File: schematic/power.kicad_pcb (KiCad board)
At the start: 2 copper layers, 76.7 x 52.7 mm, 21 parts, among them J1 Conn_01x02, J2 Conn_01x02, J3 Conn_01x02, J4 Conn_01x02, J5 Conn_02x06_Odd_Even, U1 LM2595S-3.3, U2 INA219AxD

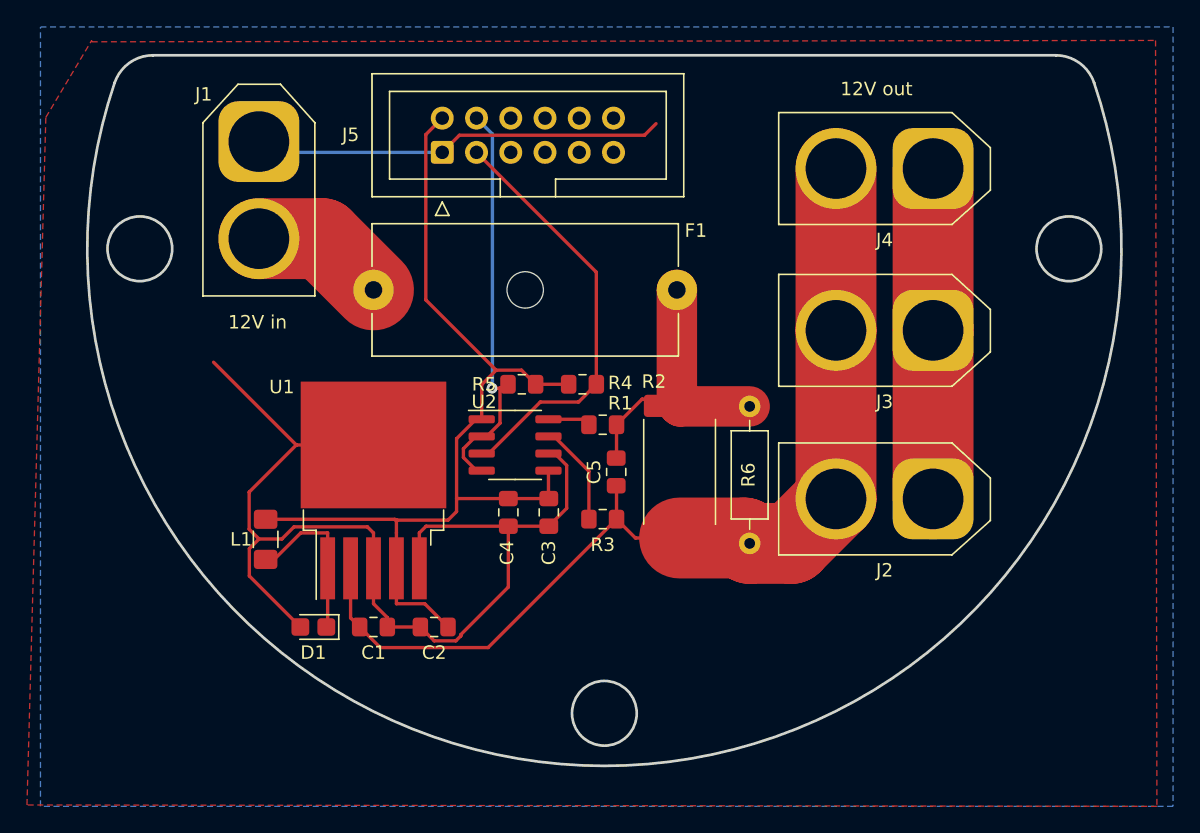
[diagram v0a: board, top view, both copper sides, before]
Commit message: correct power D1, C1, C2 and L1 footprint. accurate L1, D1 and C2 values
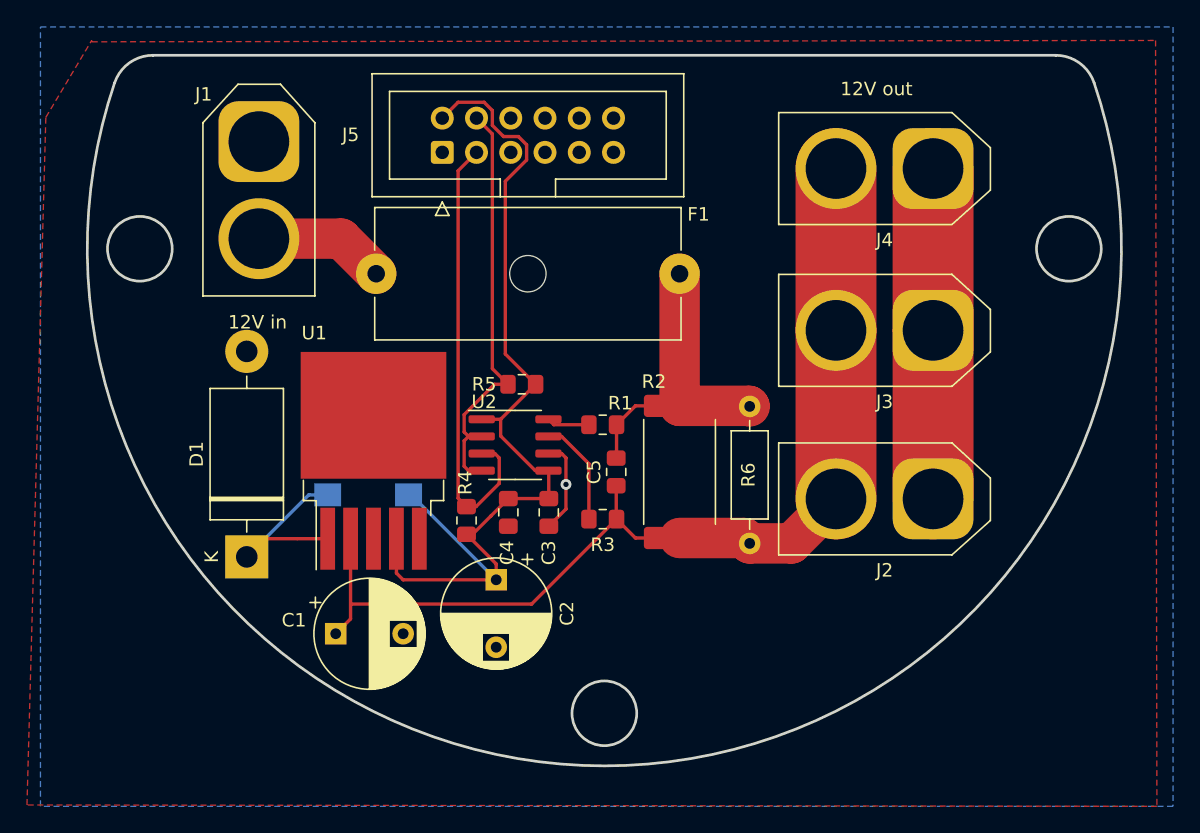
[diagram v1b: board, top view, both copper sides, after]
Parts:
- C1: value C680uF -> CP; footprint Capacitor_SMD:C_0805_2012Metric_Pad1.15x1.40mm_HandSolder -> Capacitor_THT:CP_Radial_D8.0mm_P5.00mm
- C2: footprint Capacitor_SMD:C_0805_2012Metric_Pad1.15x1.40mm_HandSolder -> Capacitor_THT:CP_Radial_D8.0mm_P5.00mm
- D1: value D -> 1N5822; footprint Diode_SMD:D_0805_2012Metric_Castellated -> Diode_THT:D_DO-201AD_P15.24mm_Horizontal
- L1: value L33uH -> 68uH; footprint Inductor_SMD:L_1206_3216Metric_Pad1.42x1.75mm_HandSolder -> Inductor_SMD:L_Wuerth_WE-PD-Typ-7345; moved to B.Cu
- moved R4 13.3 mm to (142.9, 114.6), turned to 270 degrees
- moved L1 8.29 mm to (135.6, 112.7), turned to 0 degrees
- moved D1 7.17 mm to (126.6, 117.3), turned to 90 degrees
- moved C2 5.78 mm to (145.1, 119.0), turned to 270 degrees
- moved C1 2.84 mm to (133.2, 123.0)
- moved U1 2.20 mm to (136.0, 110.2)
- moved F1 1.22 mm to (158.7, 96.3)
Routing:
- net GND: track 138.0 -> 31.5 mm, vias 0 -> 1
- net I2C-SDA: track 31.5 -> 33.6 mm
- net Net-(D1-Pad1): track 12.4 -> 14.5 mm
- net +12V: track 73.6 -> 75.2 mm
- net +3V3: track 73.2 -> 71.8 mm
- net Net-(C5-Pad2): track 21.6 -> 22.8 mm
- net I2C-SCL: track 30.3 -> 31.4 mm, vias 1 -> 0
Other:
- board text added: "Aruna power github.com/aruna-rov"
- board text removed: "Aruna power github.com/aruna"

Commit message: added version
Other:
- board text added: "Aruna - Power github.com/aruna-rov/Apsu V1"
- board text removed: "Aruna power github.com/aruna-rov"

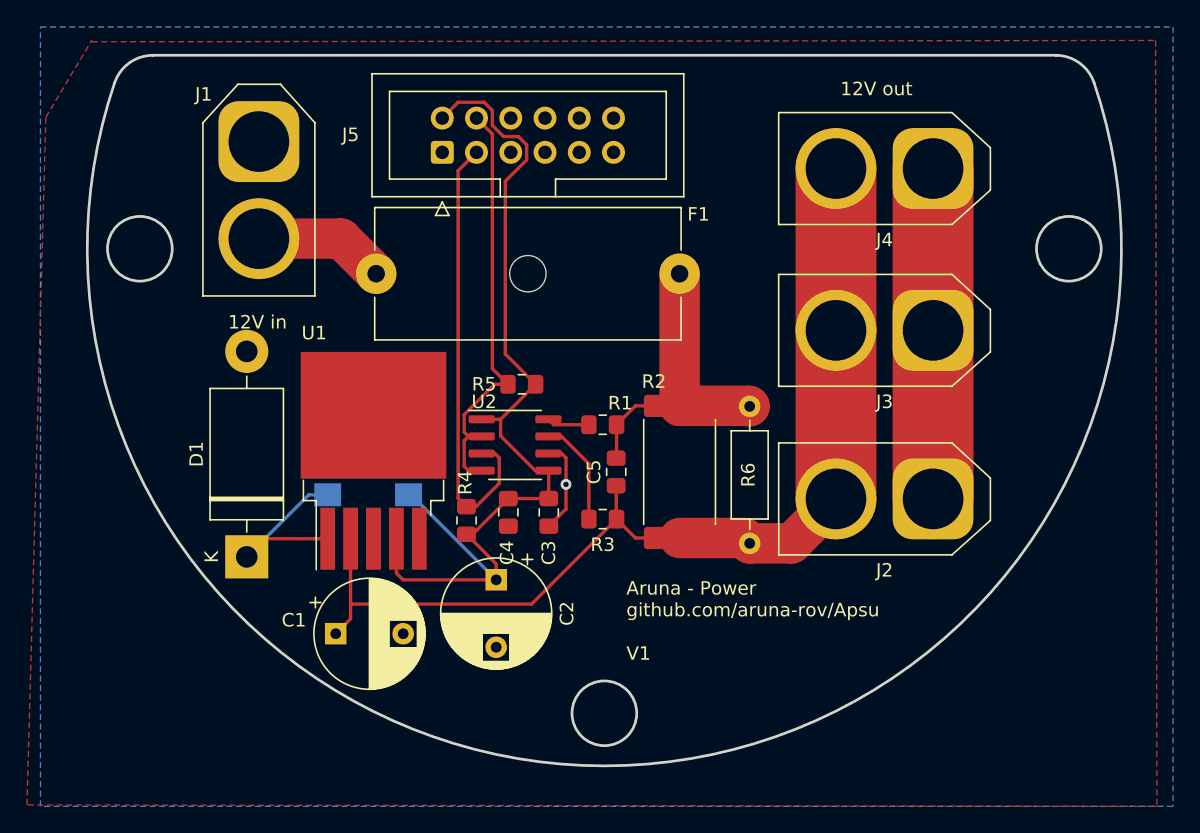
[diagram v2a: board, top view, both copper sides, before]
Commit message: added MPN for connectors
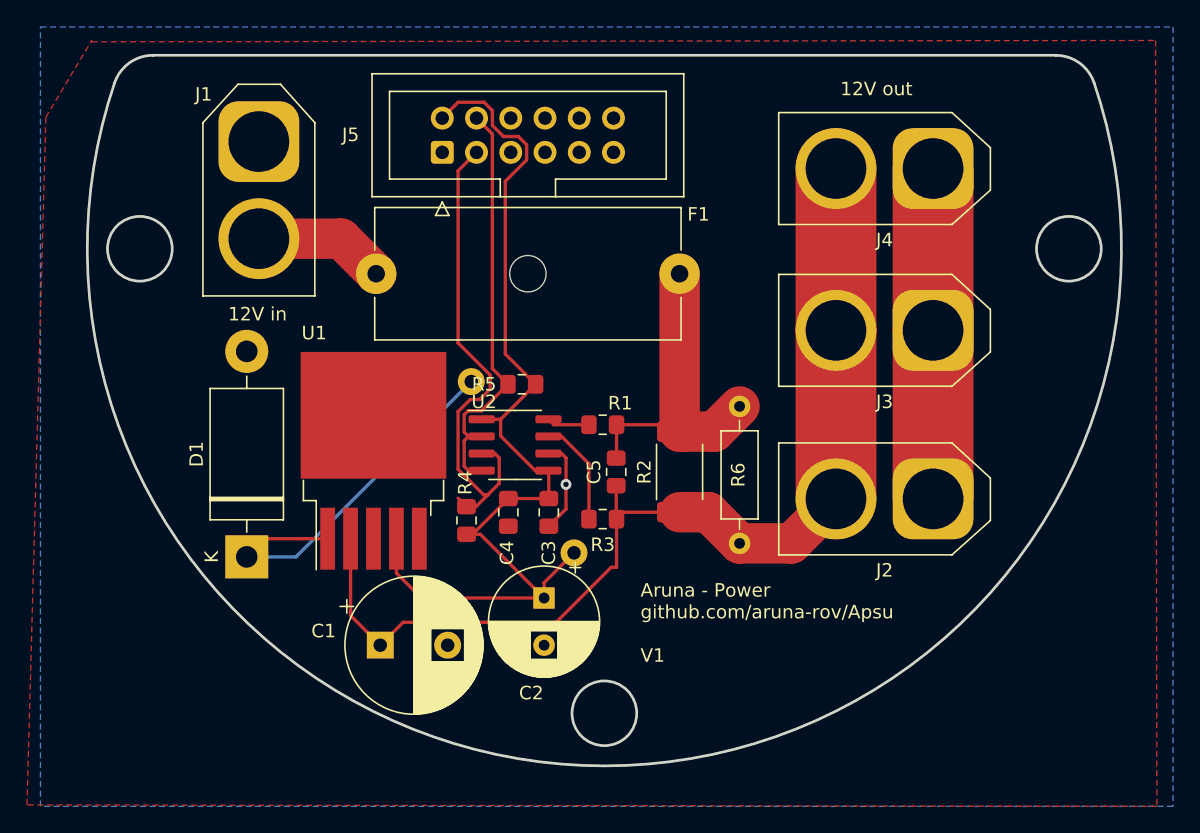
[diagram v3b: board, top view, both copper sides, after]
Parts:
- C1: value CP -> 100uF; footprint Capacitor_THT:CP_Radial_D8.0mm_P5.00mm -> Capacitor_THT:CP_Radial_D10.0mm_P5.00mm
- C2: value C220uF -> 220uF; footprint Capacitor_THT:CP_Radial_D8.0mm_P5.00mm -> Capacitor_THT:CP_Radial_D8.0mm_P3.50mm
- L1: footprint Inductor_SMD:L_Wuerth_WE-PD-Typ-7345 -> Inductor_THT:L_Radial_L16.1mm_W16.1mm_Px7.62mm_Py12.70mm_Pulse_LP-44
- R2: footprint Resistor_SMD:R_4020_10251Metric_Pad1.65x5.30mm_HandSolder -> Resistor_SMD:R_2512_6332Metric_Pad1.52x3.35mm_HandSolder
- moved L1 11.4 mm to (143.2, 104.3)
- moved C2 3.80 mm to (148.7, 120.3)
- moved C1 3.41 mm to (136.5, 123.8)
- moved R6 0.75 mm to (163.2, 116.3)
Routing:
- net Net-(D1-Pad1): track 14.5 -> 28.6 mm
- net I2C-SDA: track 33.6 -> 36.8 mm
- net +12V: track 75.2 -> 78.1 mm
- net +3V3: track 71.8 -> 74.5 mm
- net Net-(C5-Pad2): track 22.8 -> 24.3 mm
